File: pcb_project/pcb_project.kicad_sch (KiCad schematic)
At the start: 0 parts

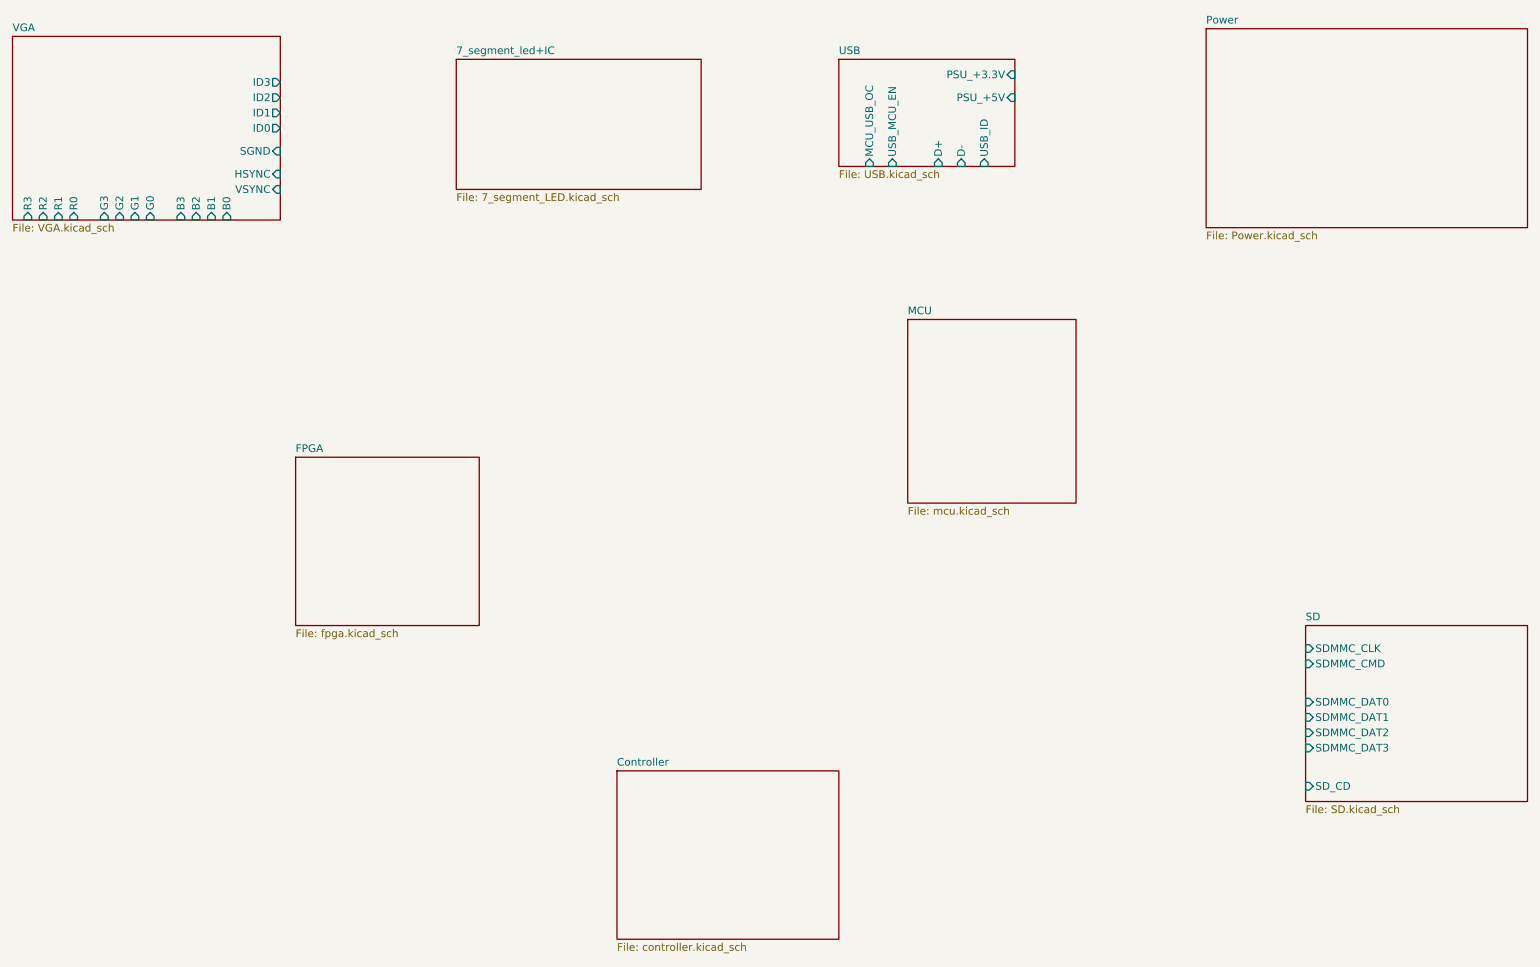
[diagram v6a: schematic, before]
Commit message: Sync sheet pins
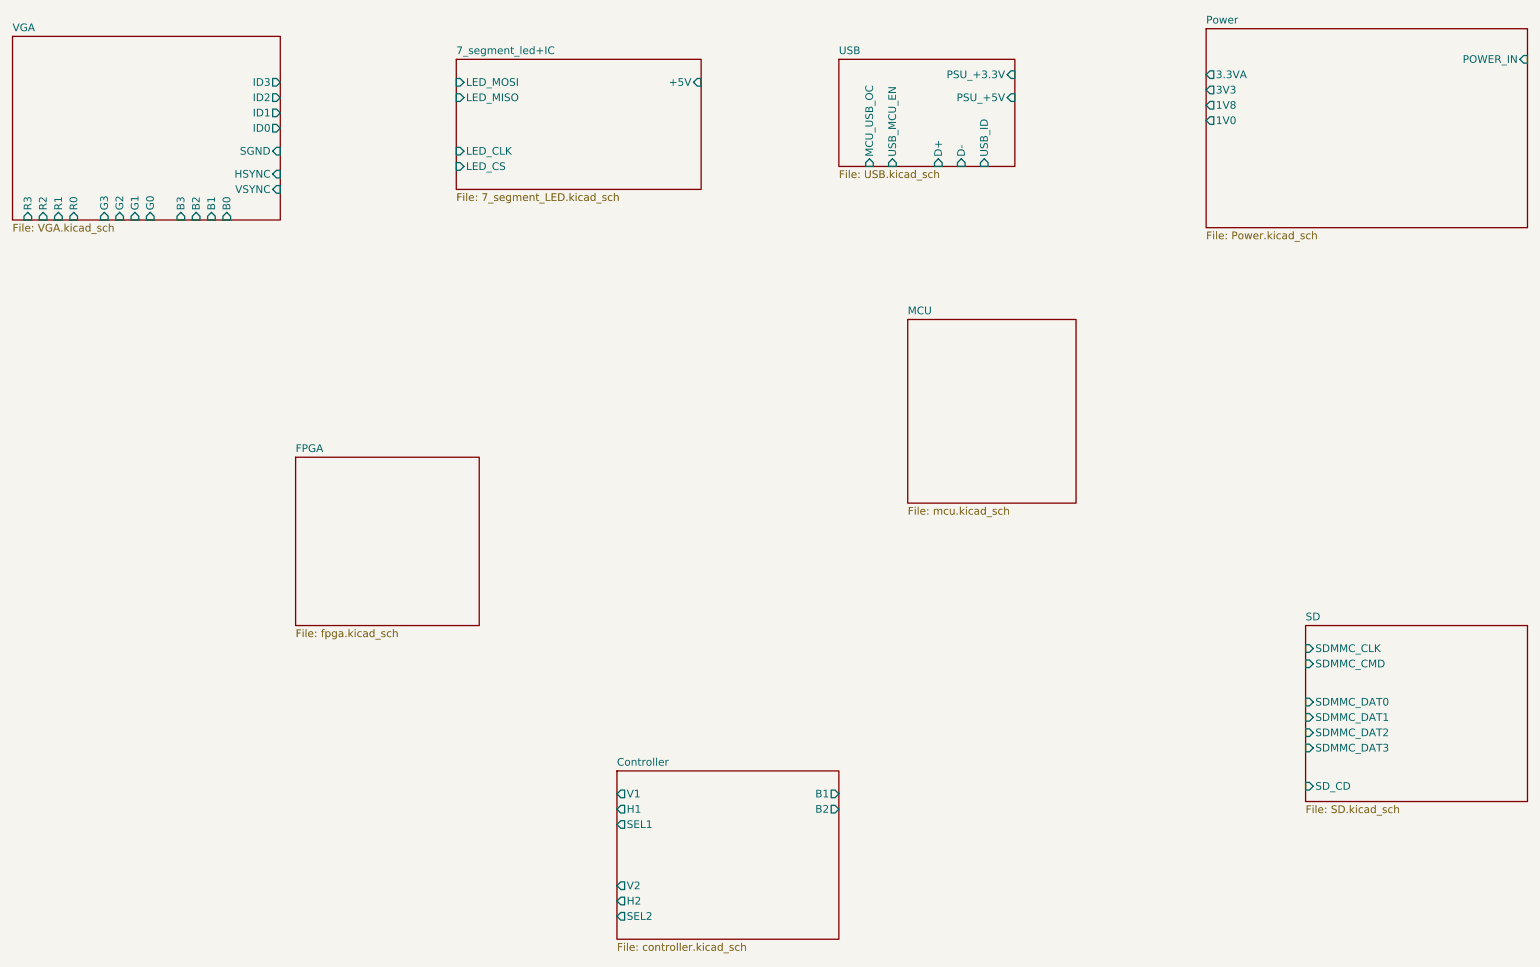
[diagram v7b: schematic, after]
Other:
- sheet 7_segment_led+IC ports: added +5V, LED_CLK, LED_CS, LED_MISO, LED_MOSI; removed none
- sheet Controller ports: added B1, B2, H1, H2, SEL1, SEL2, V1, V2; removed none
- sheet Power ports: added 1V0, 1V8, 3.3VA, 3V3, POWER_IN; removed none
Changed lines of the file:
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@@
+			)
+		)
+		(pin "LED_MOSI" input
+			(at 99.06 30.48 180)
+			(effects
+				(font
+					(size 1.27 1.27)
+				)
+				(justify left)
+			)
+		)
+		(pin "LED_CS" input
+			(at 99.06 44.45 180)
+			(effects
+				(font
+					(size 1.27 1.27)
+				)
+				(justify left)
+			)
+		)
+		(pin "LED_CLK" input
+			(at 99.06 41.91 180)
+			(effects
+				(font
+					(size 1.27 1.27)
+				)
+				(justify left)
+			)
+		)
+		(pin "+5V" input
+			(at 139.7 30.48 0)
+			(effects
+				(font
+					(size 1.27 1.27)
+				)
+				(justify right)
+			)
+		)
+		(pin "LED_MISO" input
+			(at 99.06 33.02 180)
+			(effects
+				(font
+					(size 1.27 1.27)
+				)
+				(justify left)
 			)
 		)
@@
 			)
 		)
+		(pin "B1" output
+			(at 162.56 148.59 0)
+			(effects
+				(font
+					(size 1.27 1.27)
+				)
+				(justify right)
+			)
+		)
+		(pin "V1" output
+			(at 125.73 148.59 180)
+			(effects
+				(font
+					(size 1.27 1.27)
+				)
+				(justify left)
+			)
+		)
+		(pin "SEL2" output
+			(at 125.73 168.91 180)
+			(effects
+				(font
+					(size 1.27 1.27)
+				)
+				(justify left)
+			)
+		)
+		(pin "SEL1" output
+			(at 125.73 153.67 180)
+			(effects
+				(font
+					(size 1.27 1.27)
+				)
+				(justify left)
+			)
+		)
+		(pin "H1" output
+			(at 125.73 151.13 180)
+			(effects
+				(font
+					(size 1.27 1.27)
+				)
+				(justify left)
+			)
+		)
+		(pin "H2" output
+			(at 125.73 166.37 180)
+			(effects
+				(font
+					(size 1.27 1.27)
+				)
+				(justify left)
+			)
+		)
+		(pin "B2" output
+			(at 162.56 151.13 0)
+			(effects
+				(font
+					(size 1.27 1.27)
+				)
+				(justify right)
+			)
+		)
+		(pin "V2" output
+			(at 125.73 163.83 180)
+			(effects
+				(font
+					(size 1.27 1.27)
+				)
+				(justify left)
+			)
+		)
 		(instances
 			(project "pcb_project"
@@
 			)
 		)
+		(pin "POWER_IN" input
+			(at 276.86 26.67 0)
+			(effects
+				(font
+					(size 1.27 1.27)
+				)
+				(justify right)
+			)
+		)
+		(pin "3V3" output
+			(at 223.52 31.75 180)
+			(effects
+				(font
+					(size 1.27 1.27)
+				)
+				(justify left)
+			)
+		)
+		(pin "1V0" output
+			(at 223.52 36.83 180)
+			(effects
+				(font
+					(size 1.27 1.27)
+				)
+				(justify left)
+			)
+		)
+		(pin "3.3VA" output
+			(at 223.52 29.21 180)
+			(effects
+				(font
+					(size 1.27 1.27)
+				)
+				(justify left)
+			)
+		)
+		(pin "1V8" output
+			(at 223.52 34.29 180)
+			(effects
+				(font
+					(size 1.27 1.27)
+				)
+				(justify left)
+			)
+		)

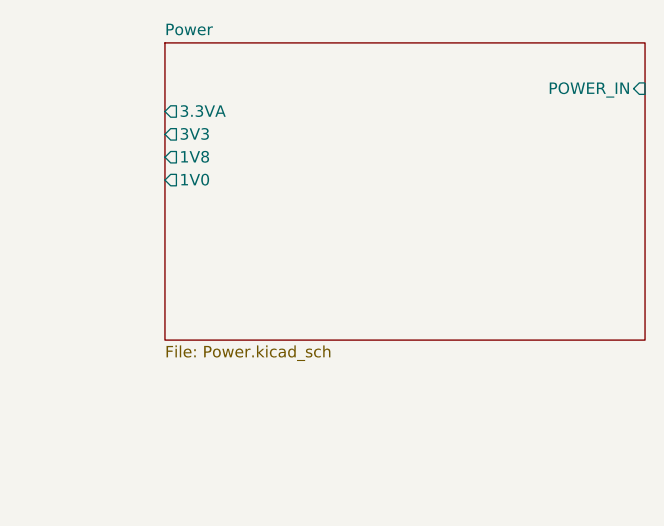
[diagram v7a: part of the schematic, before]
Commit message: Add MicroUSB as power input
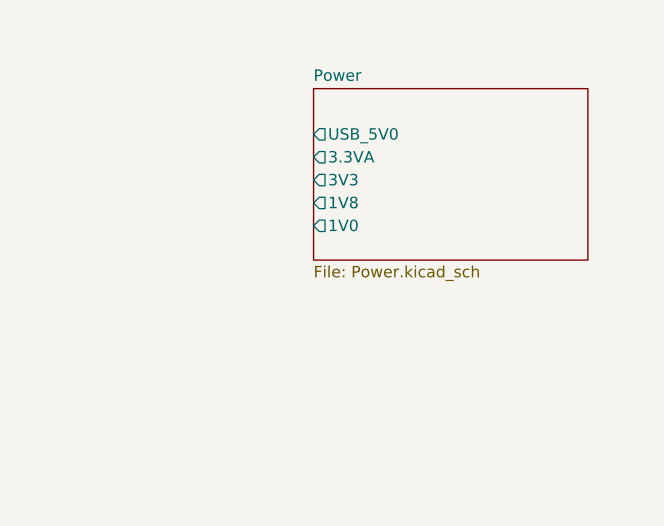
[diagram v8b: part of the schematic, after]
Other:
- sheet Power ports: added USB_5V0; removed POWER_IN
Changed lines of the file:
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@@
 	)
 	(sheet
-		(at 223.52 21.59)
-		(size 53.34 33.02)
+		(at 240.03 26.67)
+		(size 30.48 19.05)
 		(exclude_from_sim no)
 		(in_bom yes)
@@
 		)
 		(property "Sheetname" "Power"
-			(at 223.52 20.8784 0)
+			(at 240.03 25.9584 0)
 			(effects
 				(font
@@
 		)
 		(property "Sheetfile" "Power.kicad_sch"
-			(at 223.52 55.1946 0)
+			(at 240.03 46.3046 0)
 			(effects
 				(font
@@
 			)
 		)
-		(pin "POWER_IN" input
-			(at 276.86 26.67 0)
-			(effects
-				(font
-					(size 1.27 1.27)
-				)
-				(justify right)
-			)
-		)
 		(pin "3V3" output
-			(at 223.52 31.75 180)
+			(at 240.03 36.83 180)
 			(effects
 				(font
@@
 		)
 		(pin "1V0" output
-			(at 223.52 36.83 180)
+			(at 240.03 41.91 180)
 			(effects
 				(font
@@
 		)
 		(pin "3.3VA" output
-			(at 223.52 29.21 180)
+			(at 240.03 34.29 180)
 			(effects
 				(font
@@
 		)
 		(pin "1V8" output
-			(at 223.52 34.29 180)
+			(at 240.03 39.37 180)
 			(effects
 				(font
+					(size 1.27 1.27)
+				)
+				(justify left)
+			)
+		)
+		(pin "USB_5V0" output
+			(at 240.03 31.75 180)
+			(effects
+				(font
